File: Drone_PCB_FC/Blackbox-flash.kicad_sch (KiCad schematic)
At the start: 5 parts, among them U7 W25Q128JVE

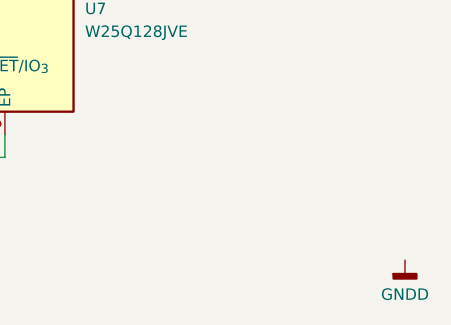
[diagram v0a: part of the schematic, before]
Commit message: almost done with the schmatic design
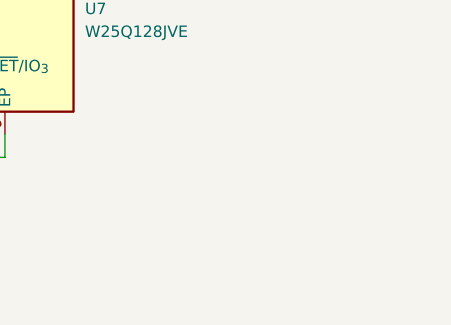
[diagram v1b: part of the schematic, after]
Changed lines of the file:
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@@
-	)
-	(symbol
-		(lib_id "power:GNDD")
-		(at 181.61 123.19 0)
-		(unit 1)
-		(body_style 1)
-		(exclude_from_sim no)
-		(in_bom yes)
-		(on_board yes)
-		(in_pos_files yes)
-		(dnp no)
-		(fields_autoplaced yes)
-		(property "Reference" "#PWR047"
-			(at 181.61 129.54 0)
-			(hide yes)
-			(show_name no)
-			(do_not_autoplace no)
-			(effects
-				(font
-					(size 1.27 1.27)
-				)
-			)
-		)
-		(property "Value" "GNDD"
-			(at 181.61 127 0)
-			(show_name no)
-			(do_not_autoplace no)
-			(effects
-				(font
-					(size 1.27 1.27)
-				)
-			)
-		)
-		(property "Footprint" ""
-			(at 181.61 123.19 0)
-			(hide yes)
-			(show_name no)
-			(do_not_autoplace no)
-			(effects
-				(font
-					(size 1.27 1.27)
-				)
-			)
-		)
-		(property "Datasheet" ""
-			(at 181.61 123.19 0)
-			(hide yes)
-			(show_name no)
-			(do_not_autoplace no)
-			(effects
-				(font
-					(size 1.27 1.27)
-				)
-			)
-		)
-		(property "Description" "Power symbol creates a global label with name \"GNDD\" , digital ground"
-			(at 181.61 123.19 0)
-			(hide yes)
-			(show_name no)
-			(do_not_autoplace no)
-			(effects
-				(font
-					(size 1.27 1.27)
-				)
-			)
-		)
-		(pin "1"
-		)
-		(instances
-			(project "Drone_PCB_FC"
-				(path "/30482008-3d6c-427d-9917-9811da561e6b/04903022-eede-422e-95a9-23de68cd321e"
-					(reference "#PWR047")
-					(unit 1)
-				)
-			)
-		)
 	)
 	(symbol
